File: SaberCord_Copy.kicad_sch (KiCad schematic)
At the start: 2 parts, among them J1 Conn_02x07_Counter_Clockwise, J3 USB_C_Receptacle

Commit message: push before eod
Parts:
- removed J3: USB_C_Receptacle, Connector_USB:USB_C_Receptacle_Amphenol_12401610E4-2A_CircularHoles, symbol Connector:USB_C_Receptacle
- added J2: USB_C_Receptacle, Connector_USB:USB_C_Receptacle_Amphenol_12401548E4-2A_CircularHoles, symbol Connector:USB_C_Receptacle
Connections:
- net at J1.14 (Pin_14): now also J2.A4 (VBUS), J2.A9 (VBUS), J2.B4 (VBUS), J2.B9 (VBUS)
- net at J1.8 (Pin_8): now also J2.A1 (GND), J2.A12 (GND), J2.B1 (GND), J2.B12 (GND)
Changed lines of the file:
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@@
 (kicad_sch (version 20230121) (generator eeschema)
   (paper "A4")
-  (symbol (lib_id "Connector:USB_C_Receptacle") (at 207.01 85.09 0) (mirror y) (unit 1)
+  (wire (pts (xy 198.12 118.11) (xy 161.29 118.11))
+    (stroke (width 0) (type default))
+  )
+  (wire (pts (xy 161.29 52.07) (xy 161.29 69.85))
+    (stroke (width 0) (type default))
+  )
+  (wire (pts (xy 161.29 118.11) (xy 161.29 85.09))
+    (stroke (width 0) (type default))
+  )
+  (wire (pts (xy 182.88 52.07) (xy 161.29 52.07))
+    (stroke (width 0) (type default))
+  )
+  (symbol (lib_id "Connector:USB_C_Receptacle") (at 198.12 77.47 0) (mirror y) (unit 1)
     (in_bom yes) (on_board yes) (dnp no)
-    (property "Reference" "J3" (at 207.01 52.07 0)
+    (property "Reference" "J2" (at 198.12 44.45 0)
       (effects (font (size 1.27 1.27)))
     )
-    (property "Value" "USB_C_Receptacle" (at 207.01 54.61 0)
+    (property "Value" "USB_C_Receptacle" (at 198.12 46.99 0)
       (effects (font (size 1.27 1.27)))
     )
-    (property "Footprint" "Connector_USB:USB_C_Receptacle_Amphenol_12401610E4-2A_CircularHoles" (at 203.2 85.09 0)
+    (property "Footprint" "Connector_USB:USB_C_Receptacle_Amphenol_12401548E4-2A_CircularHoles" (at 194.31 77.47 0)
       (effects (font (size 1.27 1.27)) hide)
     )
-    (property "Datasheet" "https://www.usb.org/sites/default/files/documents/usb_type-c.zip" (at 203.2 85.09 0)
+    (property "Datasheet" "https://www.usb.org/sites/default/files/documents/usb_type-c.zip" (at 194.31 77.47 0)
       (effects (font (size 1.27 1.27)) hide)
     )
@@
       (project "SaberCord_Copy"
         (path "/be2c8e72-e310-467f-9e4e-b384214483bd"
-          (reference "J3") (unit 1)
+          (reference "J2") (unit 1)
         )
       )
     )
   )
-  (symbol (lib_id "Connector_Generic:Conn_02x07_Counter_Clockwise") (at 148.59 87.63 0) (unit 1)
+  (symbol (lib_id "Connector_Generic:Conn_02x07_Counter_Clockwise") (at 153.67 77.47 0) (unit 1)
     (in_bom yes) (on_board yes) (dnp no) (fields_autoplaced)
-    (property "Reference" "J1" (at 149.86 73.66 0)
+    (property "Reference" "J1" (at 154.94 63.5 0)
+      (effects (font (size 1.27 1.27)) hide)
+    )
+    (property "Value" "Conn_02x07_Counter_Clockwise" (at 154.94 66.04 0)
       (effects (font (size 1.27 1.27)))
     )
-    (property "Value" "Conn_02x07_Counter_Clockwise" (at 149.86 76.2 0)
-      (effects (font (size 1.27 1.27)))
-    )
-    (property "Footprint" "" (at 148.59 87.63 0)
+    (property "Footprint" "" (at 153.67 77.47 0)
       (effects (font (size 1.27 1.27)) hide)
     )
-    (property "Datasheet" "~" (at 148.59 87.63 0)
+    (property "Datasheet" "~" (at 153.67 77.47 0)
       (effects (font (size 1.27 1.27)) hide)
     )

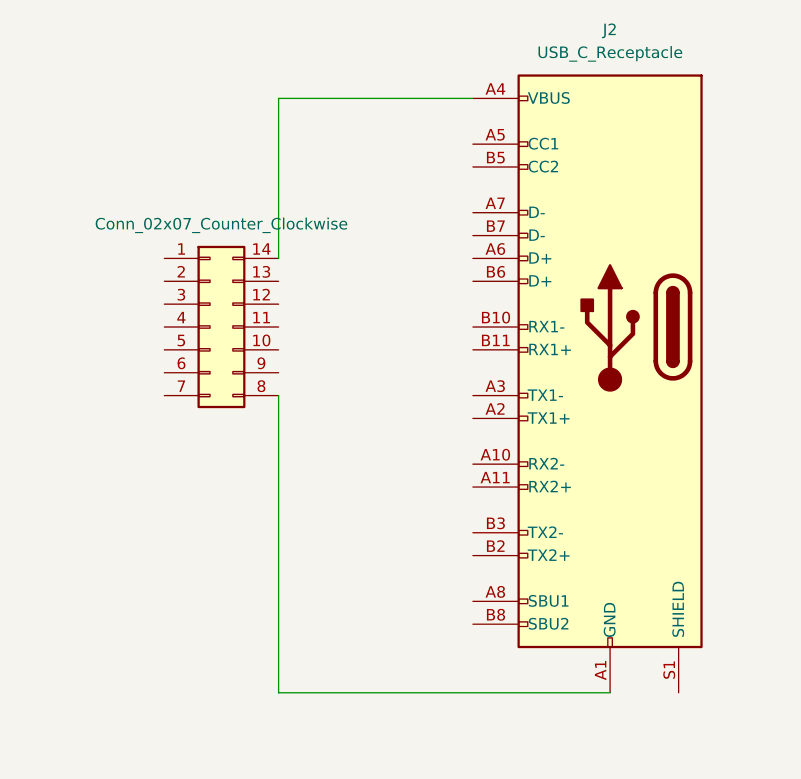
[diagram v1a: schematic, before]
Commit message: finish wiring schematic for pogo
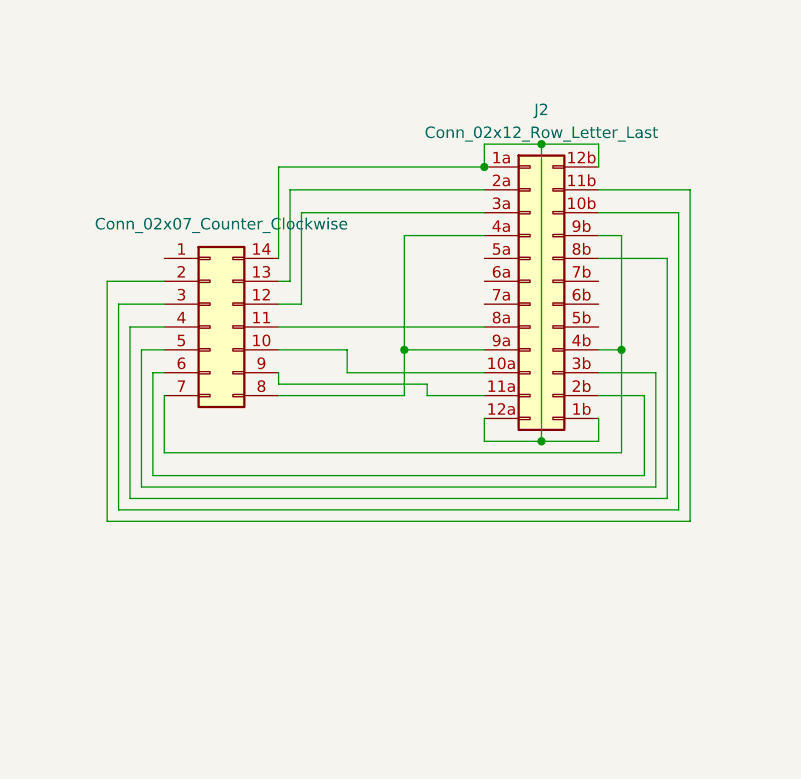
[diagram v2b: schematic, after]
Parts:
- removed J2: USB_C_Receptacle, Connector_USB:USB_C_Receptacle_Amphenol_12401548E4-2A_CircularHoles, symbol Connector:USB_C_Receptacle
- added J2: Conn_02x12_Row_Letter_Last, symbol USB_C_24P_Lettered:Conn_02x12_Row_Letter_Last
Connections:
- net at J1.8 (Pin_8): now also J2.4a (Pin_4a), J2.9a (Pin_9a)
- net at J1.14 (Pin_14): now also J2.12a (Pin_12a), J2.12b (Pin_1b), J2.1a (Pin_1a), J2.1b (Pin_12b)
- net at J1.10 (Pin_10): now also J2.10a (Pin_10a)
- net at J1.11 (Pin_11): now also J2.8a (Pin_8a)
- net at J1.12 (Pin_12): now also J2.3a (Pin_3a)
- net at J1.13 (Pin_13): now also J2.2a (Pin_2a)
- net at J1.2 (Pin_2): now also J2.11b (Pin_2b)
- net at J1.3 (Pin_3): now also J2.10b (Pin_3b)
- net at J1.4 (Pin_4): now also J2.8b (Pin_5b)
- net at J1.5 (Pin_5): now also J2.3b (Pin_10b)
- net at J1.6 (Pin_6): now also J2.2b (Pin_11b)
- net at J1.7 (Pin_7): now also J2.4b (Pin_9b), J2.9b (Pin_4b)
- net at J1.9 (Pin_9): now also J2.11a (Pin_11a)

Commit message: refine footprint and schema
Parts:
- removed J1: Conn_02x07_Counter_Clockwise, symbol Connector_Generic:Conn_02x07_Counter_Clockwise
- removed J2: Conn_02x12_Row_Letter_Last, symbol USB_C_24P_Lettered:Conn_02x12_Row_Letter_Last
- added J1: Conn_02x07_Row_Letter_Last, CommaPogo_Library:2x7_Pogo_Male, symbol Connector_Generic:Conn_02x07_Row_Letter_Last
- added J2: Conn_02x12_Row_Letter_Last, CommaPogo_Library:GCT_USB4056-03-A_REVA2, symbol Connector_Generic:Conn_02x12_Row_Letter_Last
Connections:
- new net CAN0_H: J1.2 (Pin_2a), J2.A2 (a2)
- new net CAN0_L: J1.3 (Pin_3a), J2.A3 (a3)
- new net CAN1_H: J1.6 (Pin_6a), J2.A11 (a11)
- new net CAN1_L: J1.5 (Pin_5a), J2.A10 (a10)
- new net CAN2_H: J1.9 (Pin_2b), J2.B2 (b2)
- new net CAN2_L: J1.10 (Pin_3b), J2.B3 (b3)
- new net CAN3_H: J1.12 (Pin_5b), J2.B11 (b11)
- new net CAN3_L: J1.13 (Pin_6b), J2.B10 (b10)
- new net GND: J1.1 (Pin_1a), J1.8 (Pin_1b), J2.A1 (a1), J2.A12 (a12), J2.B1 (b1), J2.B12 (b12)
- new net SBU1: J1.4 (Pin_4a), J2.A8
- new net SBU2: J1.11 (Pin_4b), J2.B8 (b8)
- new net VIN: J1.14 (Pin_7b), J1.7 (Pin_7a), J2.A4 (a4), J2.A9 (a9), J2.B4 (b4), J2.B9 (b9)
- no-connect marks 0 -> 6
